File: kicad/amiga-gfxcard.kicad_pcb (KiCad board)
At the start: 2 copper layers, 171.2 x 72.9 mm, 34 parts, among them P1 CONN_01X04, P2 CONN_01X16, P3 CONN_01X16, P4 CONN_01X16, P5 CONN_01X04, P6 CONN_01X04, P7 CONN_01X08, U1 TXB0108, U10 SN74CBT16233, U12 VGA, U2 TXB0108, U3 TXB0108, U4 TXB0108, U5 TXB0108, U6 TXB0108, U7 ADV7125-lqfp48, U8 SN74CBT16233, U9 74LS04

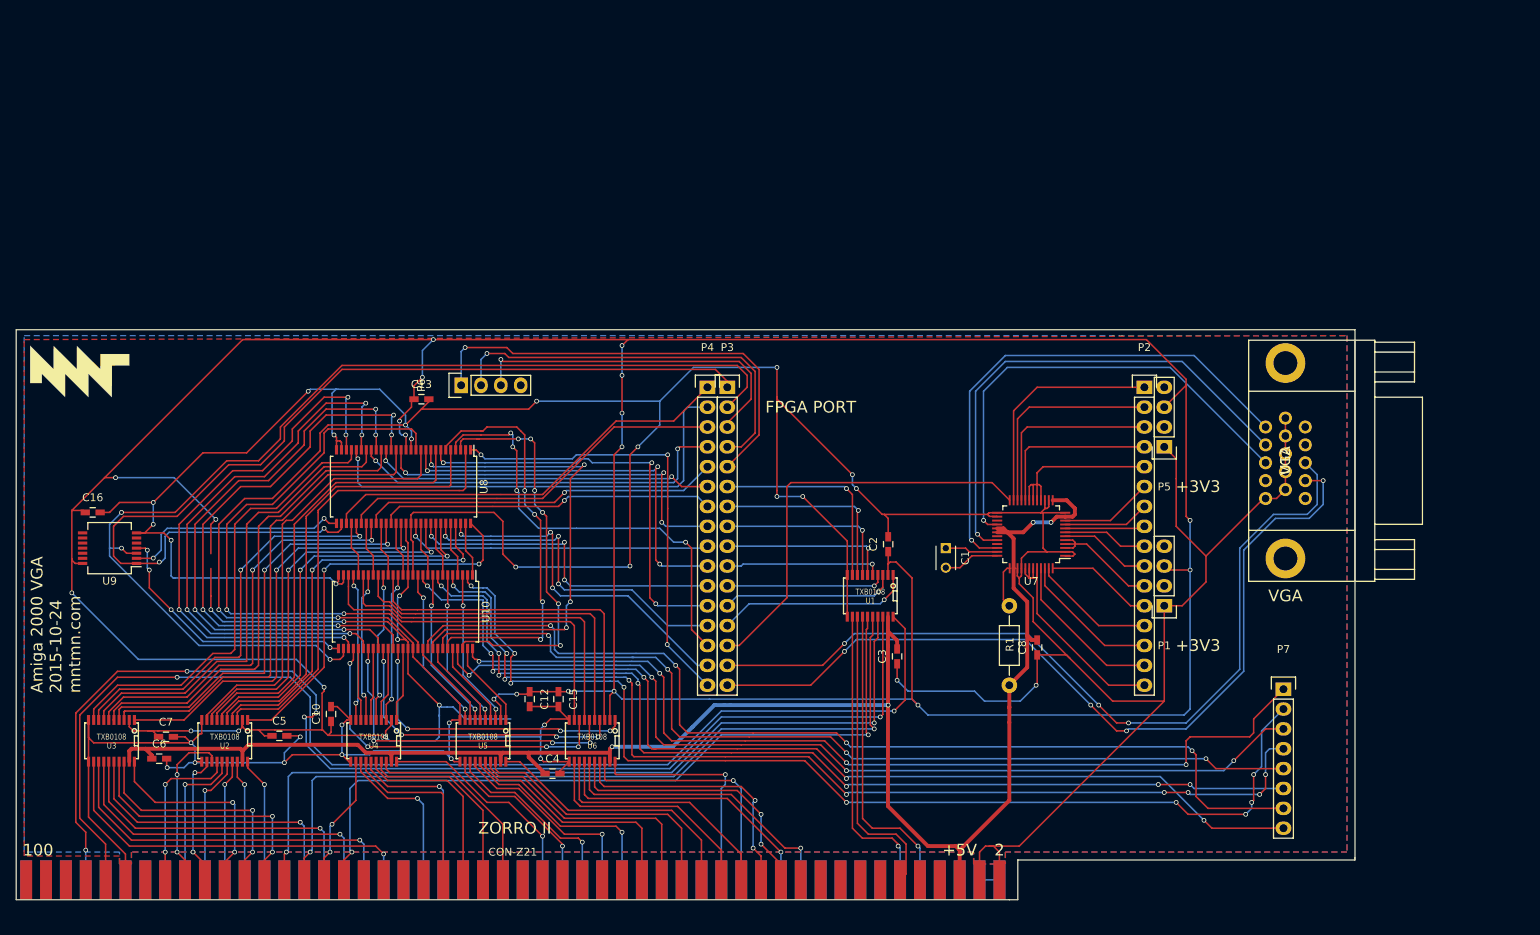
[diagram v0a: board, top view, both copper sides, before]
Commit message: WIP of simpler redesign for miniSpartan 6+
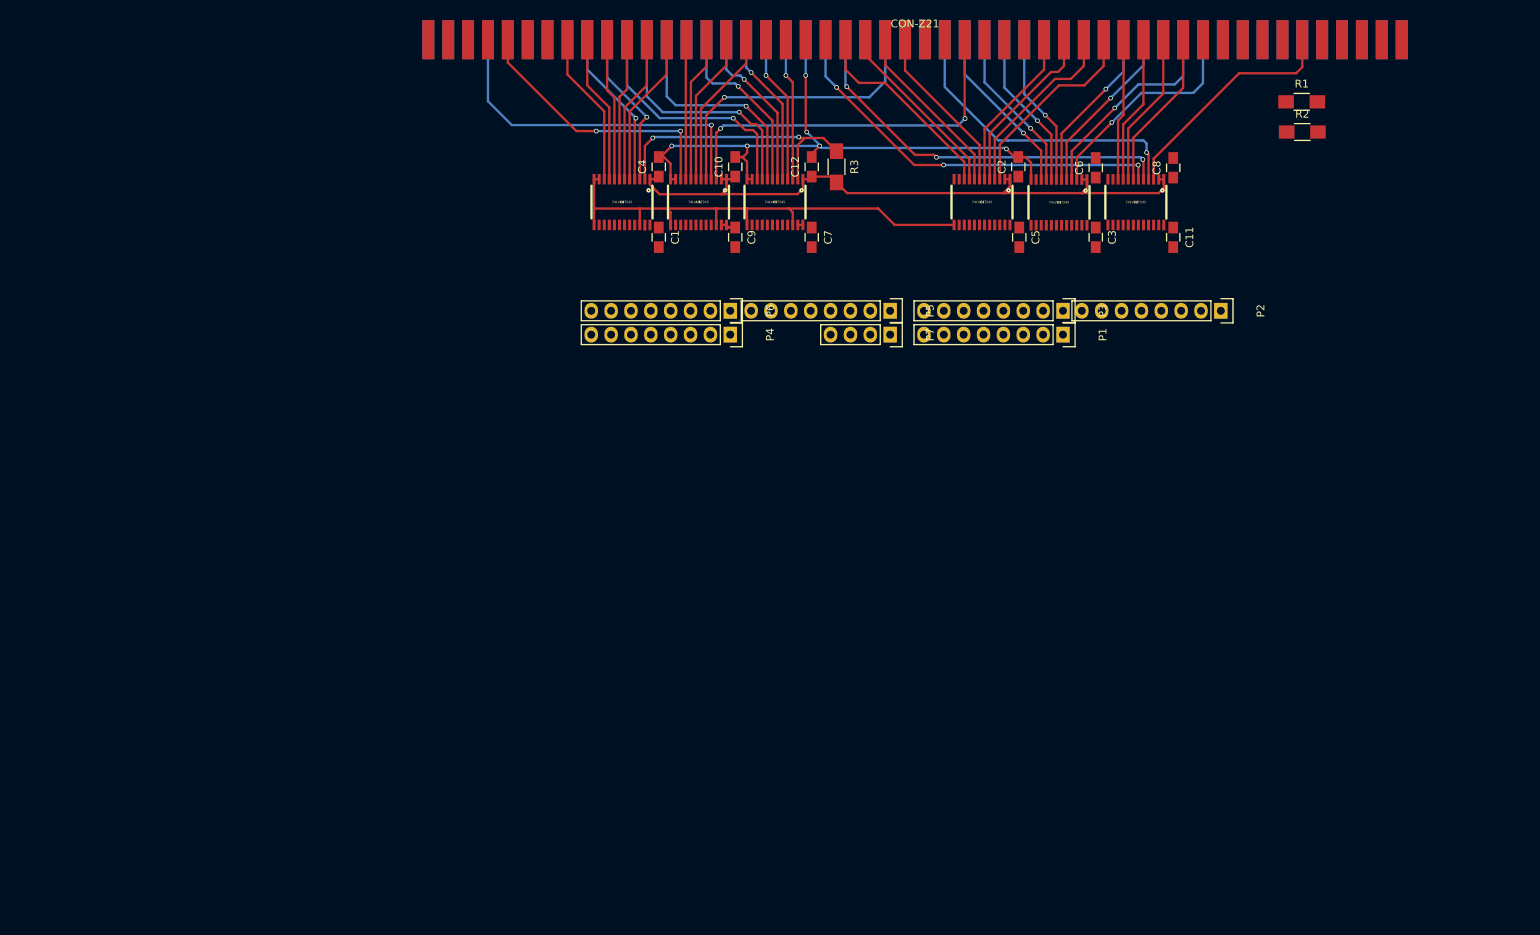
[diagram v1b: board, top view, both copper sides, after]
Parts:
- removed C13, C15, C16: C_Small, Capacitors_SMD:C_0603_HandSoldering
- removed G***: LOGO, mnt:mnt
- removed U10, U8: SN74CBT16233, Housings_SSOP:SSOP-56_7.5x18.5mm_Pitch0.635mm
- removed U12: VGA, zorro2:HD15_B-HD15F
- removed U7: ADV7125-lqfp48, Housings_QFP:LQFP-48_7x7mm_Pitch0.5mm
- removed U9: 74LS04, Housings_SSOP:SSOP-14_5.3x6.2mm_Pitch0.65mm
- added C11: .1uF, Capacitors_SMD:C_0805_HandSoldering, F.Cu at (183.5, 52.5)
- added C9: .1uF, Capacitors_SMD:C_0805_HandSoldering, F.Cu at (127.5, 52.5)
- added R2: 10k, Resistors_SMD:R_1206_HandSoldering, F.Cu at (200.0, 39.0)
- added R3: 10k, Resistors_SMD:R_1206_HandSoldering, F.Cu at (140.5, 43.4)
- C1: value 0.1uF -> .1uF; footprint Capacitors_ThroughHole:C_Disc_D3_P2.5 -> Capacitors_SMD:C_0805_HandSoldering
- C10, C12, C2, C3, C4, C5, C6, C7, C8: value C_Small -> .1uF; footprint Capacitors_SMD:C_0603_HandSoldering -> Capacitors_SMD:C_0805_HandSoldering
- P1: value CONN_01X04 -> ADDR1; footprint Pin_Headers:Pin_Header_Straight_1x04 -> Pin_Headers:Pin_Header_Straight_1x08
- P2: value CONN_01X16 -> ADDR2; footprint Pin_Headers:Pin_Header_Straight_1x16 -> Pin_Headers:Pin_Header_Straight_1x08
- P3: value CONN_01X16 -> ADDR3; footprint Pin_Headers:Pin_Header_Straight_1x16 -> Pin_Headers:Pin_Header_Straight_1x08
- P4: value CONN_01X16 -> DATA1; footprint Pin_Headers:Pin_Header_Straight_1x16 -> Pin_Headers:Pin_Header_Straight_1x08
- P5: value CONN_01X04 -> DATA2; footprint Pin_Headers:Pin_Header_Straight_1x04 -> Pin_Headers:Pin_Header_Straight_1x08
- P6: value CONN_01X04 -> CTRL_IN; footprint Pin_Headers:Pin_Header_Straight_1x04 -> Pin_Headers:Pin_Header_Straight_1x08
- P7: value CONN_01X08 -> CTRL_OUT; footprint Pin_Headers:Pin_Header_Straight_1x08 -> Pin_Headers:Pin_Header_Straight_1x04
- R1: value 82k -> 10k; footprint Resistors_ThroughHole:Resistor_Horizontal_RM10mm -> Resistors_SMD:R_1206_HandSoldering
- U1, U2, U3, U4, U5, U6: value TXB0108 -> 74LVC8T245; footprint opendous:TSSOP20_PW -> mnt:TSSOP24-44
- moved C6 141.6 mm to (173.6, 43.6), turned to 90 degrees
- moved U3 139.4 mm to (168.9, 48.0)
- moved U2 135.4 mm to (178.7, 48.0)
- moved CON-Z21 119.1 mm to (150.5, 24.6)
- moved C5 114.1 mm to (163.8, 52.5), turned to 270 degrees
- moved C7 104.4 mm to (137.3, 52.5), turned to 270 degrees
- moved C10 87.0 mm to (127.5, 43.4)
- moved R1 78.9 mm to (199.9, 35.1), turned to 0 degrees
- moved C4 78.8 mm to (117.7, 43.4), turned to 90 degrees
- moved U5 78.4 mm to (132.6, 47.9)
- moved C12 77.0 mm to (137.3, 43.4), turned to 90 degrees
- moved U4 75.9 mm to (113.0, 47.9)
- moved U6 70.2 mm to (122.8, 47.9)
- moved P7 67.7 mm to (147.3, 64.9), turned to 270 degrees
- moved C8 63.8 mm to (183.5, 43.6)
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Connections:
- C1 pad 1: Net-(C1-Pad1) -> +3V3
- C1 pad 2: Net-(C1-Pad2) -> GND
- C10 pad 1: +3V3 -> +5V
- C12 pad 1: +3V3 -> +5V
- C2 pad 1: +3V3 -> +5V
- C3 pad 1: GND -> +3V3
- C3 pad 2: +5V -> GND
- C8 pad 1: GND -> +5V
- C8 pad 2: +5V -> GND
- CON-Z21 pad 100: Net-(CON-Z21-Pad100) -> GND
- CON-Z21 pad 13: Net-(CON-Z21-Pad13) -> GND
- CON-Z21 pad 25: Net-(CON-Z21-Pad25) -> GND
- CON-Z21 pad 29: /A1 -> Net-(CON-Z21-Pad29)
- CON-Z21 pad 30: /A8 -> Net-(CON-Z21-Pad30)
- CON-Z21 pad 32: /A9 -> Net-(CON-Z21-Pad32)
- CON-Z21 pad 37: Net-(CON-Z21-Pad37) -> GND
- CON-Z21 pad 45: /A16 -> Net-(CON-Z21-Pad45)
- CON-Z21 pad 47: /A17 -> Net-(CON-Z21-Pad47)
- CON-Z21 pad 49: Net-(CON-Z21-Pad49) -> GND
- CON-Z21 pad 5: Net-(CON-Z21-Pad5) -> +5V
- CON-Z21 pad 59: /A23 -> Net-(CON-Z21-Pad59)
- CON-Z21 pad 61: Net-(CON-Z21-Pad61) -> GND
- CON-Z21 pad 63: /D15 -> Net-(CON-Z21-Pad63)
- CON-Z21 pad 70: //LDS -> Net-(CON-Z21-Pad70)
- CON-Z21 pad 72: //UDS -> Net-(CON-Z21-Pad72)
- CON-Z21 pad 73: Net-(CON-Z21-Pad73) -> GND
- CON-Z21 pad 74: //AS -> Net-(CON-Z21-Pad74)
- CON-Z21 pad 75: /D0 -> Net-(CON-Z21-Pad75)
- CON-Z21 pad 80: /D8 -> Net-(CON-Z21-Pad80)
- CON-Z21 pad 82: /D7 -> Net-(CON-Z21-Pad82)
- CON-Z21 pad 85: Net-(CON-Z21-Pad85) -> GND
- CON-Z21 pad 87: Net-(CON-Z21-Pad87) -> GND
- CON-Z21 pad 88: Net-(CON-Z21-Pad88) -> GND
- CON-Z21 pad 89: Net-(CON-Z21-Pad89) -> GND
- CON-Z21 pad 99: Net-(CON-Z21-Pad99) -> GND
- P1 pad 1: GND -> Net-(P1-Pad1)
- P1 pad 3: +3V3 -> Net-(P1-Pad3)
- P5 pad 1: GND -> Net-(P5-Pad1)
- P5 pad 3: +3V3 -> Net-(P5-Pad3)
- P6 pad 1: Net-(P3-Pad5) -> Net-(P6-Pad1)
- P6 pad 2: Net-(P3-Pad4) -> Net-(P6-Pad2)
- P6 pad 3: Net-(P3-Pad3) -> Net-(P6-Pad3)
- P7 pad 1: Net-(P7-Pad1) -> Net-(CON-Z21-Pad9)
- P7 pad 2: Net-(P7-Pad2) -> Net-(CON-Z21-Pad11)
- R1 pad 1: Net-(R1-Pad1) -> Net-(CON-Z21-Pad11)
- U1 pad 1: Net-(P3-Pad13) -> +5V
- U1 pad 10: GND -> Net-(CON-Z21-Pad58)
- U1 pad 12: Net-(CON-Z21-Pad11) -> GND
- U1 pad 13: Net-(CON-Z21-Pad12) -> GND
- U1 pad 14: Net-(CON-Z21-Pad9) -> Net-(P1-Pad8)
- U1 pad 15: Net-(CON-Z21-Pad68) -> Net-(P1-Pad7)
- U1 pad 16: //UDS -> Net-(P1-Pad6)
- U1 pad 17: //AS -> Net-(P1-Pad5)
- U1 pad 18: Net-(CON-Z21-Pad93) -> Net-(P1-Pad4)
- U1 pad 19: +5V -> Net-(P1-Pad3)
- U1 pad 2: +3V3 -> +5V
- U1 pad 20: Net-(CON-Z21-Pad92) -> Net-(P1-Pad2)
- U1 pad 3: Net-(P3-Pad12) -> Net-(CON-Z21-Pad32)
- U1 pad 4: Net-(P3-Pad11) -> Net-(CON-Z21-Pad34)
- U1 pad 5: Net-(P3-Pad10) -> Net-(CON-Z21-Pad36)
- U1 pad 6: Net-(P3-Pad9) -> Net-(CON-Z21-Pad38)
- U1 pad 7: Net-(P3-Pad8) -> Net-(CON-Z21-Pad52)
- U1 pad 8: Net-(P3-Pad7) -> Net-(CON-Z21-Pad54)
- U1 pad 9: Net-(P3-Pad6) -> Net-(CON-Z21-Pad56)
- U2 pad 1: Net-(U2-Pad1) -> +5V
- U2 pad 10: GND -> Net-(CON-Z21-Pad30)
- U2 pad 12: /D7 -> GND
- U2 pad 13: Net-(CON-Z21-Pad84) -> GND
- U2 pad 14: Net-(CON-Z21-Pad86) -> Net-(P2-Pad8)
- U2 pad 15: Net-(CON-Z21-Pad83) -> Net-(P2-Pad7)
- U2 pad 16: Net-(CON-Z21-Pad81) -> Net-(P2-Pad6)
- U2 pad 17: Net-(CON-Z21-Pad79) -> Net-(P2-Pad5)
- U2 pad 18: Net-(CON-Z21-Pad77) -> Net-(P2-Pad4)
- U2 pad 19: +5V -> Net-(P2-Pad3)
- U2 pad 2: +3V3 -> +5V
- U2 pad 20: /D0 -> Net-(P2-Pad2)
- U2 pad 3: Net-(U2-Pad3) -> Net-(CON-Z21-Pad12)
- U2 pad 4: Net-(U2-Pad4) -> Net-(CON-Z21-Pad47)
- U2 pad 5: Net-(U2-Pad5) -> Net-(CON-Z21-Pad57)
- U2 pad 6: Net-(U2-Pad6) -> Net-(CON-Z21-Pad59)
- U2 pad 7: Net-(U2-Pad7) -> Net-(CON-Z21-Pad24)
- U2 pad 8: Net-(U2-Pad8) -> Net-(CON-Z21-Pad26)
- U2 pad 9: Net-(U2-Pad9) -> Net-(CON-Z21-Pad28)
- U3 pad 1: Net-(U3-Pad1) -> +5V
- U3 pad 10: GND -> Net-(CON-Z21-Pad45)
- U3 pad 12: /D15 -> GND
- U3 pad 13: Net-(CON-Z21-Pad65) -> GND
- U3 pad 14: Net-(CON-Z21-Pad67) -> Net-(P3-Pad8)
- U3 pad 15: Net-(CON-Z21-Pad69) -> Net-(P3-Pad7)
- U3 pad 16: Net-(CON-Z21-Pad71) -> Net-(P3-Pad6)
- U3 pad 17: Net-(CON-Z21-Pad76) -> Net-(P3-Pad5)
- U3 pad 18: Net-(CON-Z21-Pad78) -> Net-(P3-Pad4)
- U3 pad 19: +5V -> Net-(P3-Pad3)
- U3 pad 2: +3V3 -> +5V
- U3 pad 20: /D8 -> Net-(P3-Pad2)
- U3 pad 3: Net-(U3-Pad3) -> Net-(CON-Z21-Pad21)
- U3 pad 4: Net-(U3-Pad4) -> Net-(CON-Z21-Pad23)
- U3 pad 5: Net-(U3-Pad5) -> Net-(CON-Z21-Pad27)
- U3 pad 6: Net-(U3-Pad6) -> Net-(CON-Z21-Pad29)
- U3 pad 7: Net-(U3-Pad7) -> Net-(CON-Z21-Pad39)
- U3 pad 8: Net-(U3-Pad8) -> Net-(CON-Z21-Pad41)
- U3 pad 9: Net-(U3-Pad9) -> Net-(CON-Z21-Pad43)
- U4 pad 1: Net-(U10-Pad42) -> +5V
- U4 pad 10: GND -> Net-(CON-Z21-Pad86)
- U4 pad 12: //LDS -> GND
- U4 pad 13: /A23 -> GND
- U4 pad 14: Net-(CON-Z21-Pad58) -> Net-(P4-Pad8)
- U4 pad 15: Net-(CON-Z21-Pad57) -> Net-(P4-Pad7)
- U4 pad 16: Net-(CON-Z21-Pad56) -> Net-(P4-Pad6)
- U4 pad 17: Net-(CON-Z21-Pad54) -> Net-(P4-Pad5)
- U4 pad 18: Net-(CON-Z21-Pad52) -> Net-(P4-Pad4)
- U4 pad 19: +5V -> Net-(P4-Pad3)
- U4 pad 2: +3V3 -> Net-(P7-Pad3)
- U4 pad 20: /A17 -> Net-(P4-Pad2)
- U4 pad 3: Net-(U10-Pad16) -> Net-(CON-Z21-Pad81)
- U4 pad 4: Net-(U10-Pad39) -> Net-(CON-Z21-Pad83)
- U4 pad 5: Net-(U10-Pad19) -> Net-(CON-Z21-Pad76)
- U4 pad 6: Net-(U10-Pad36) -> Net-(CON-Z21-Pad78)
- U4 pad 7: Net-(U10-Pad22) -> Net-(CON-Z21-Pad80)
- U4 pad 8: Net-(U10-Pad33) -> Net-(CON-Z21-Pad82)
- U4 pad 9: Net-(U10-Pad25) -> Net-(CON-Z21-Pad84)
- U5 pad 1: Net-(U10-Pad55) -> +5V
- U5 pad 10: GND -> Net-(CON-Z21-Pad79)
- U5 pad 12: /A16 -> GND
- U5 pad 13: Net-(CON-Z21-Pad43) -> GND
- U5 pad 14: Net-(CON-Z21-Pad41) -> Net-(P5-Pad8)
- U5 pad 15: Net-(CON-Z21-Pad39) -> Net-(P5-Pad7)
- U5 pad 16: Net-(CON-Z21-Pad38) -> Net-(P5-Pad6)
- U5 pad 17: Net-(CON-Z21-Pad36) -> Net-(P5-Pad5)
- U5 pad 18: Net-(CON-Z21-Pad34) -> Net-(P5-Pad4)
- U5 pad 19: +5V -> Net-(P5-Pad3)
- U5 pad 2: +3V3 -> Net-(P7-Pad3)
- U5 pad 20: /A9 -> Net-(P5-Pad2)
- U5 pad 3: Net-(U10-Pad3) -> Net-(CON-Z21-Pad63)
- U5 pad 4: Net-(U10-Pad52) -> Net-(CON-Z21-Pad65)
- U5 pad 5: Net-(U10-Pad6) -> Net-(CON-Z21-Pad67)
- U5 pad 6: Net-(U10-Pad49) -> Net-(CON-Z21-Pad69)
- U5 pad 7: Net-(U10-Pad9) -> Net-(CON-Z21-Pad71)
- U5 pad 8: Net-(U10-Pad46) -> Net-(CON-Z21-Pad75)
- U5 pad 9: Net-(U10-Pad12) -> Net-(CON-Z21-Pad77)
- U6 pad 1: Net-(U10-Pad41) -> +5V
- U6 pad 10: GND -> Net-(CON-Z21-Pad92)
- U6 pad 12: /A8 -> GND
- U6 pad 13: Net-(CON-Z21-Pad28) -> GND
- U6 pad 14: Net-(CON-Z21-Pad23) -> Net-(P6-Pad8)
- U6 pad 15: Net-(CON-Z21-Pad21) -> Net-(P6-Pad7)
- U6 pad 16: Net-(CON-Z21-Pad24) -> Net-(P6-Pad6)
- U6 pad 17: Net-(CON-Z21-Pad26) -> Net-(P6-Pad5)
- U6 pad 18: Net-(CON-Z21-Pad27) -> Net-(P6-Pad4)
- U6 pad 19: +5V -> Net-(P6-Pad3)
- U6 pad 2: +3V3 -> +5V
- U6 pad 20: /A1 -> Net-(P6-Pad2)
- U6 pad 3: Net-(U10-Pad17) -> Net-(CON-Z21-Pad46)
- U6 pad 4: Net-(U10-Pad38) -> Net-(CON-Z21-Pad93)
- U6 pad 5: Net-(U10-Pad20) -> Net-(CON-Z21-Pad53)
- U6 pad 6: Net-(U10-Pad35) -> Net-(CON-Z21-Pad68)
- U6 pad 7: Net-(U10-Pad23) -> Net-(CON-Z21-Pad70)
- U6 pad 8: Net-(U10-Pad32) -> Net-(CON-Z21-Pad72)
- U6 pad 9: Net-(U10-Pad26) -> Net-(CON-Z21-Pad74)
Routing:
- net +3V3: track 588.9 -> 3.20 mm, vias 27 -> 0
- net GND: track 708.3 -> 143.8 mm, vias 32 -> 6
- net Net-(P3-Pad2): track 140.8 -> 0.00 mm, vias 3 -> 0
- net Net-(P7-Pad2): track 139.4 -> 0.00 mm, vias 9 -> 0
- net +5V: track 220.4 -> 82.3 mm, vias 4 -> 0
- net Net-(P7-Pad4): track 134.8 -> 0.00 mm, vias 9 -> 0
- net Net-(P7-Pad8): track 134.0 -> 0.00 mm, vias 6 -> 0
- net Net-(P7-Pad6): track 130.3 -> 0.00 mm, vias 7 -> 0
- net Net-(P7-Pad7): track 129.6 -> 0.00 mm, vias 4 -> 0
- net Net-(P3-Pad1): track 127.2 -> 0.00 mm, vias 2 -> 0
- net Net-(P7-Pad5): track 121.7 -> 0.00 mm, vias 4 -> 0
- net Net-(P7-Pad1): track 121.5 -> 0.00 mm, vias 4 -> 0
- net Net-(CON-Z21-Pad92): track 152.9 -> 34.8 mm
- net Net-(P3-Pad16): track 109.9 -> 0.00 mm, vias 4 -> 0
- net Net-(CON-Z21-Pad93): track 154.1 -> 44.6 mm, vias 5 -> 1
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- removed copper zone on B.Cu, net GND
- removed copper zone on F.Cu, net GND
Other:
- board outline removed
- net class Default: trace_width 0.2 -> 0.3
- board text removed: "+3V3"
- board text removed: "+5V"
- board text removed: "100"
- board text removed: "2"
- board text removed: "Amiga 2000 VGA 2015-10-24 mntmn.com"
- board text removed: "FPGA PORT"
- board text removed: "VGA"
- board text removed: "ZORRO II"

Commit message: WIP new PCB
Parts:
- moved P7 10.3 mm to (137.0, 64.4)
- moved P1 1.97 mm to (167.5, 64.4)
- moved P3 1.91 mm to (167.5, 61.8)
- moved P2 1.78 mm to (187.8, 61.8)
- moved P4 0.51 mm to (126.9, 64.4)
- moved P5 0.13 mm to (147.2, 61.8)
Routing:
- net Net-(CON-Z21-Pad11): track 0.00 -> 102.0 mm, vias 0 -> 3
- net Net-(CON-Z21-Pad9): track 0.00 -> 98.4 mm, vias 0 -> 3
- net +3V3: track 3.20 -> 88.7 mm, vias 0 -> 7
- net +5V: track 82.3 -> 140.6 mm, vias 0 -> 1
- net GND: track 143.8 -> 190.3 mm, vias 6 -> 7
- net Net-(P7-Pad3): track 35.6 -> 62.7 mm, vias 2 -> 3
- net Net-(P3-Pad8): track 0.00 -> 25.9 mm
- net Net-(P3-Pad7): track 0.00 -> 24.0 mm
- net Net-(P3-Pad6): track 0.00 -> 21.9 mm
- net Net-(P6-Pad8): track 0.00 -> 20.8 mm
- net Net-(P3-Pad5): track 0.00 -> 19.9 mm
- net Net-(P5-Pad1): track 0.00 -> 19.8 mm
- net Net-(P4-Pad1): track 0.00 -> 19.7 mm, vias 0 -> 1
- net Net-(P6-Pad7): track 0.00 -> 18.8 mm
- net Net-(P5-Pad2): track 0.00 -> 18.3 mm
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
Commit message: redo of mk2 board finished
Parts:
- added P10: AUX1B, Pin_Headers:Pin_Header_Straight_1x08, F.Cu at (111.5, 48.8)
- added P11: AUX2A, Pin_Headers:Pin_Header_Straight_1x04, F.Cu at (132.1, 48.8)
- added P12: AUX2B, Pin_Headers:Pin_Header_Straight_1x04, F.Cu at (132.1, 40.6)
- added P8: CONN_01X02, Pin_Headers:Pin_Header_Straight_1x02, F.Cu at (108.6, 67.1)
- added P9: AUX1A, Pin_Headers:Pin_Header_Straight_1x08, F.Cu at (111.5, 40.6)
- P3: value ADDR3 -> ADDR4
- P4: value DATA1 -> DATA2
- P5: value DATA2 -> ADDR3
- P6: value CTRL_IN -> DATA1
- moved U5 73.2 mm to (203.7, 65.2), turned to 0 degrees
- moved CON-Z21 68.1 mm to (164.7, 91.2)
- moved C12 67.4 mm to (198.9, 70.9), turned to 270 degrees
- moved C7 62.1 mm to (198.9, 60.7), turned to 90 degrees
- moved R2 48.5 mm to (216.7, 84.6)
- moved R1 48.2 mm to (216.7, 80.4)
- moved C8 37.2 mm to (156.9, 69.5), turned to 270 degrees
- moved P2 36.8 mm to (152.6, 51.2), turned to 90 degrees
- moved C2 29.3 mm to (176.7, 69.7), turned to 270 degrees
- moved R3 29.1 mm to (153.7, 69.3), turned to 90 degrees
- moved P5 28.9 mm to (172.9, 48.8), turned to 90 degrees
- moved U1 28.2 mm to (181.4, 65.2), turned to 0 degrees
- moved C11 27.8 mm to (156.9, 60.6), turned to 90 degrees
- moved C10 27.7 mm to (136.1, 69.7), turned to 270 degrees
- moved C6 26.8 mm to (166.8, 69.5), turned to 270 degrees
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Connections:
- P7 pad 1: Net-(CON-Z21-Pad9) -> Net-(CON-Z21-Pad11)
- P7 pad 2: Net-(CON-Z21-Pad11) -> Net-(CON-Z21-Pad9)
- R3 pad 1: Net-(P7-Pad3) -> Net-(P7-Pad4)
- U1 pad 10: Net-(CON-Z21-Pad58) -> Net-(CON-Z21-Pad21)
- U1 pad 3: Net-(CON-Z21-Pad32) -> Net-(CON-Z21-Pad45)
- U1 pad 4: Net-(CON-Z21-Pad34) -> Net-(CON-Z21-Pad43)
- U1 pad 5: Net-(CON-Z21-Pad36) -> Net-(CON-Z21-Pad41)
- U1 pad 6: Net-(CON-Z21-Pad38) -> Net-(CON-Z21-Pad39)
- U1 pad 7: Net-(CON-Z21-Pad52) -> Net-(CON-Z21-Pad29)
- U1 pad 8: Net-(CON-Z21-Pad54) -> Net-(CON-Z21-Pad27)
- U1 pad 9: Net-(CON-Z21-Pad56) -> Net-(CON-Z21-Pad23)
- U2 pad 10: Net-(CON-Z21-Pad30) -> Net-(CON-Z21-Pad47)
- U2 pad 2: +5V -> Net-(P7-Pad4)
- U2 pad 4: Net-(CON-Z21-Pad47) -> Net-(CON-Z21-Pad46)
- U2 pad 5: Net-(CON-Z21-Pad57) -> Net-(CON-Z21-Pad53)
- U2 pad 6: Net-(CON-Z21-Pad59) -> Net-(CON-Z21-Pad92)
- U2 pad 7: Net-(CON-Z21-Pad24) -> Net-(CON-Z21-Pad93)
- U2 pad 8: Net-(CON-Z21-Pad26) -> Net-(CON-Z21-Pad59)
- U2 pad 9: Net-(CON-Z21-Pad28) -> Net-(CON-Z21-Pad57)
- U3 pad 10: Net-(CON-Z21-Pad45) -> Net-(CON-Z21-Pad52)
- U3 pad 3: Net-(CON-Z21-Pad21) -> Net-(CON-Z21-Pad74)
- U3 pad 4: Net-(CON-Z21-Pad23) -> Net-(CON-Z21-Pad72)
- U3 pad 5: Net-(CON-Z21-Pad27) -> Net-(CON-Z21-Pad70)
- U3 pad 6: Net-(CON-Z21-Pad29) -> Net-(CON-Z21-Pad68)
- U3 pad 7: Net-(CON-Z21-Pad39) -> Net-(CON-Z21-Pad58)
- U3 pad 8: Net-(CON-Z21-Pad41) -> Net-(CON-Z21-Pad56)
- U3 pad 9: Net-(CON-Z21-Pad43) -> Net-(CON-Z21-Pad54)
- U4 pad 10: Net-(CON-Z21-Pad86) -> Net-(CON-Z21-Pad76)
- U4 pad 2: Net-(P7-Pad3) -> Net-(P7-Pad4)
- U4 pad 3: Net-(CON-Z21-Pad81) -> Net-(CON-Z21-Pad83)
- U4 pad 4: Net-(CON-Z21-Pad83) -> Net-(CON-Z21-Pad81)
- U4 pad 5: Net-(CON-Z21-Pad76) -> Net-(CON-Z21-Pad86)
- U4 pad 6: Net-(CON-Z21-Pad78) -> Net-(CON-Z21-Pad84)
- U4 pad 7: Net-(CON-Z21-Pad80) -> Net-(CON-Z21-Pad82)
- U4 pad 8: Net-(CON-Z21-Pad82) -> Net-(CON-Z21-Pad80)
- U4 pad 9: Net-(CON-Z21-Pad84) -> Net-(CON-Z21-Pad78)
- U5 pad 10: Net-(CON-Z21-Pad79) -> Net-(CON-Z21-Pad24)
- U5 pad 2: Net-(P7-Pad3) -> +5V
- U5 pad 3: Net-(CON-Z21-Pad63) -> Net-(CON-Z21-Pad38)
- U5 pad 4: Net-(CON-Z21-Pad65) -> Net-(CON-Z21-Pad36)
- U5 pad 5: Net-(CON-Z21-Pad67) -> Net-(CON-Z21-Pad34)
- U5 pad 6: Net-(CON-Z21-Pad69) -> Net-(CON-Z21-Pad32)
- U5 pad 7: Net-(CON-Z21-Pad71) -> Net-(CON-Z21-Pad30)
- U5 pad 8: Net-(CON-Z21-Pad75) -> Net-(CON-Z21-Pad28)
- U5 pad 9: Net-(CON-Z21-Pad77) -> Net-(CON-Z21-Pad26)
- U6 pad 10: Net-(CON-Z21-Pad92) -> Net-(CON-Z21-Pad63)
- U6 pad 3: Net-(CON-Z21-Pad46) -> Net-(CON-Z21-Pad79)
- U6 pad 4: Net-(CON-Z21-Pad93) -> Net-(CON-Z21-Pad77)
- U6 pad 5: Net-(CON-Z21-Pad53) -> Net-(CON-Z21-Pad75)
- U6 pad 6: Net-(CON-Z21-Pad68) -> Net-(CON-Z21-Pad71)
- U6 pad 7: Net-(CON-Z21-Pad70) -> Net-(CON-Z21-Pad69)
- U6 pad 8: Net-(CON-Z21-Pad72) -> Net-(CON-Z21-Pad67)
- U6 pad 9: Net-(CON-Z21-Pad74) -> Net-(CON-Z21-Pad65)
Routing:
- net GND: track 190.3 -> 296.8 mm, vias 7 -> 11
- net Net-(P7-Pad4): track 0.00 -> 70.5 mm, vias 0 -> 2
- net Net-(P7-Pad3): track 62.7 -> 0.00 mm, vias 3 -> 0
- net Net-(CON-Z21-Pad12): track 30.0 -> 69.9 mm, vias 0 -> 2
- net Net-(P1-Pad1): track 0.00 -> 37.9 mm, vias 0 -> 1
- net Net-(CON-Z21-Pad92): track 34.8 -> 71.7 mm, vias 2 -> 4
- net Net-(CON-Z21-Pad74): track 17.9 -> 53.8 mm
- net Net-(P1-Pad2): track 0.00 -> 35.8 mm, vias 0 -> 1
- net Net-(P1-Pad3): track 0.00 -> 33.8 mm, vias 0 -> 1
- net Net-(CON-Z21-Pad72): track 18.7 -> 51.8 mm
- net Net-(P1-Pad4): track 0.00 -> 31.9 mm, vias 0 -> 1
- net +3V3: track 88.7 -> 118.4 mm
- net Net-(CON-Z21-Pad70): track 19.4 -> 49.2 mm
- net Net-(P1-Pad5): track 0.00 -> 29.7 mm, vias 0 -> 1
- net Net-(P1-Pad6): track 0.00 -> 27.7 mm, vias 0 -> 1
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- added copper zone on B.Cu, net GND
- added copper zone on F.Cu, net GND
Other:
- board outline added: 127 x 59.1 mm
